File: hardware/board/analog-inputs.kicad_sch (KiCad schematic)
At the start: 17 parts, among them U5 MCP6002

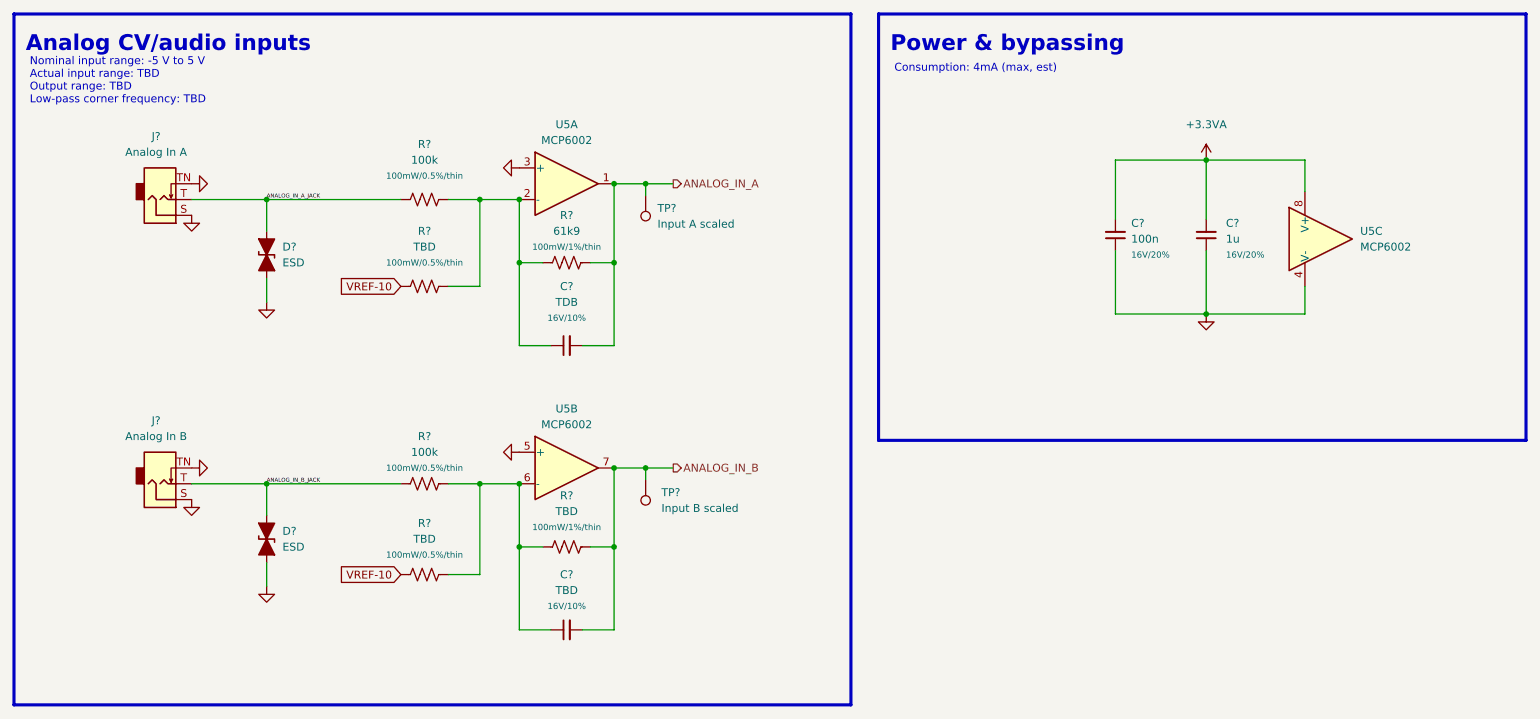
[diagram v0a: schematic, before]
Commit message: hardware: change USB connector, change flash chip, change SPI flash pin assignments, other small updates to routing
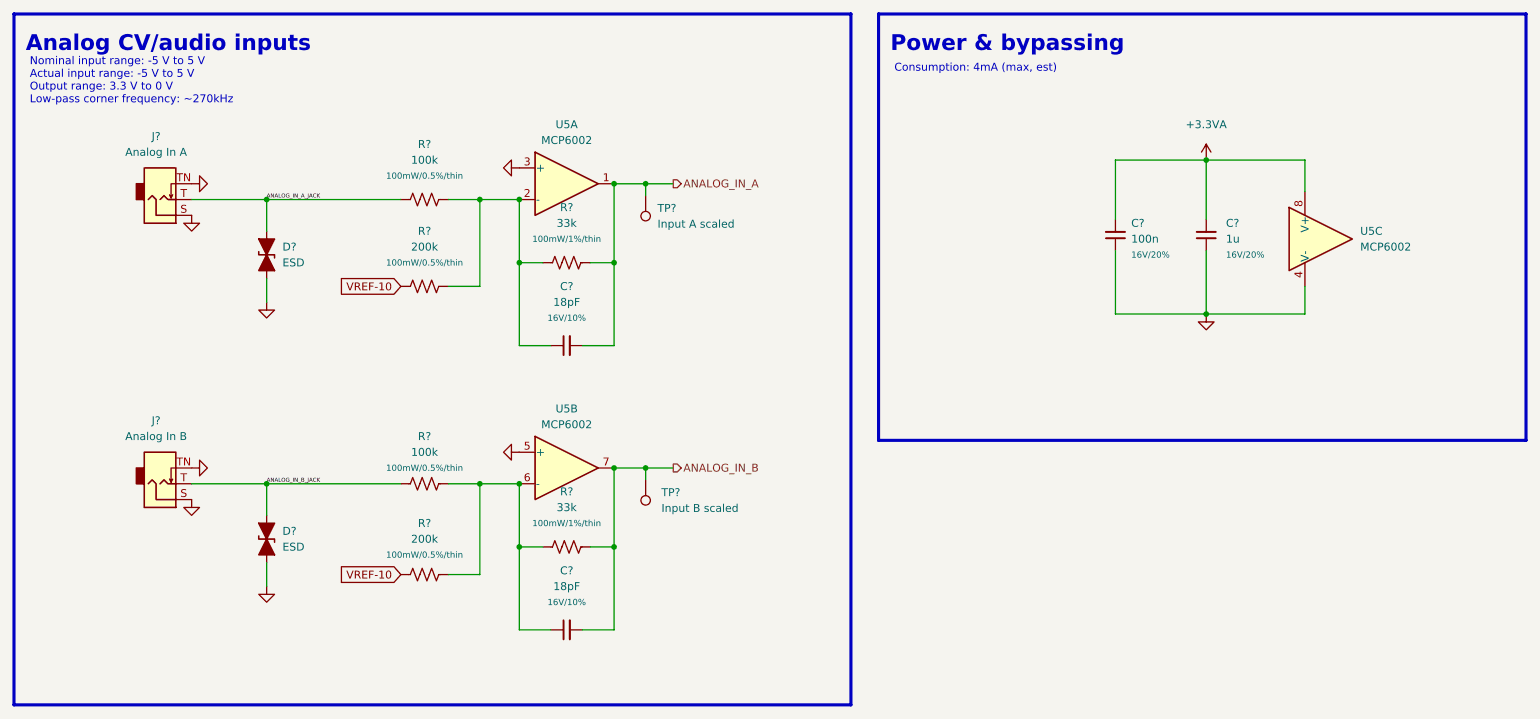
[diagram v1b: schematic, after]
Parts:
- C?: value TDB -> 18pF
- C?: value TBD -> 18pF
- R?: value TBD -> 33k
- R? (x2): value TBD -> 200k
- R?: value 61k9 -> 33k
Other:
- note added: "Nominal input range: -5 V to 5 V Actual input range: -5 V to 5 V Output range: 3.3 V to 0 V Low-pass corner frequency: ~270kHz"
- note removed: "Nominal input range: -5 V to 5 V Actual input range: TBD Output range: TBD Low-pass corner frequency: TBD"
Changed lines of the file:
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@@
     (stroke (width 0) (type default))
   )
-  (text "Nominal input range: -5 V to 5 V\nActual input range: TBD\nOutput range: TBD\nLow-pass corner frequency: TBD\n"
+  (text "Nominal input range: -5 V to 5 V\nActual input range: -5 V to 5 V\nOutput range: 3.3 V to 0 V\nLow-pass corner frequency: ~270kHz\n"
     (at 17.78 29.21 0)
     (effects (font (size 1.27 1.27)) (justify left bottom))
@@
       (effects (font (size 1.27 1.27)))
     )
-    (property "Value" "TDB" (at 104.1463 60.96 90)
+    (property "Value" "18pF" (at 104.1463 60.96 90)
       (effects (font (size 1.27 1.27)))
     )
@@
   (symbol (lib_id "Device:C_Small") (at 104.14 113.665 90) (unit 1)
     (in_bom yes) (on_board yes) (dnp no) (fields_autoplaced)
-    (property "Reference" "C?" (at 104.1463 104.775 90)
-      (effects (font (size 1.27 1.27)))
-    )
-    (property "Value" "TBD" (at 104.1463 107.315 90)
+    (property "Reference" "C?" (at 104.1463 104.14 90)
+      (effects (font (size 1.27 1.27)))
+    )
+    (property "Value" "18pF" (at 104.1463 106.68 90)
       (effects (font (size 1.27 1.27)))
     )
@@
       (effects (font (size 1.27 1.27)) hide)
     )
-    (property "Rating" "16V/10%" (at 104.1463 109.855 90)
+    (property "Rating" "16V/10%" (at 104.1463 109.22 90)
       (effects (font (size 1 1)))
     )
@@
   (symbol (lib_id "Device:R_US") (at 104.14 100.33 270) (unit 1)
     (in_bom yes) (on_board yes) (dnp no) (fields_autoplaced)
-    (property "Reference" "R?" (at 104.14 92.075 90)
-      (effects (font (size 1.27 1.27)))
-    )
-    (property "Value" "TBD" (at 104.14 94.615 90)
+    (property "Reference" "R?" (at 104.14 91.44 90)
+      (effects (font (size 1.27 1.27)))
+    )
+    (property "Value" "33k" (at 104.14 93.98 90)
       (effects (font (size 1.27 1.27)))
     )
@@
       (effects (font (size 1.27 1.27)) hide)
     )
-    (property "Rating" "100mW/1%/thin" (at 104.14 97.155 90)
+    (property "Rating" "100mW/1%/thin" (at 104.14 96.52 90)
       (effects (font (size 1 1)))
     )
@@
       (effects (font (size 1.27 1.27)))
     )
-    (property "Value" "TBD" (at 81.28 99.06 90)
+    (property "Value" "200k" (at 81.28 99.06 90)
       (effects (font (size 1.27 1.27)))
     )
@@
   (symbol (lib_id "Device:R_US") (at 104.14 54.61 270) (unit 1)
     (in_bom yes) (on_board yes) (dnp no) (fields_autoplaced)
-    (property "Reference" "R?" (at 104.14 46.99 90)
-      (effects (font (size 1.27 1.27)))
-    )
-    (property "Value" "61k9" (at 104.14 49.53 90)
+    (property "Reference" "R?" (at 104.14 45.72 90)
+      (effects (font (size 1.27 1.27)))
+    )
+    (property "Value" "33k" (at 104.14 48.26 90)
       (effects (font (size 1.27 1.27)))
     )
@@
       (effects (font (size 1.27 1.27)) hide)
     )
-    (property "Rating" "100mW/1%/thin" (at 104.14 52.07 90)
+    (property "Rating" "100mW/1%/thin" (at 104.14 50.8 90)
       (effects (font (size 1 1)))
     )
@@
       (effects (font (size 1.27 1.27)))
     )
-    (property "Value" "TBD" (at 81.28 52.07 90)
-      (effects (font (size 1.27 1.27)))
-    )
+    (property "Value" "200k" (at 81.28 52.07 90)
+      (effects (font (size 1.27 1.27)))
+    )

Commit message: hardware: rename to Goosehonk Nebula, prep v7
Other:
- title: Big Honking Button -> Goosehonk Nebula
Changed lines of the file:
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@@
   (paper "USLetter")
   (title_block
-    (title "Big Honking Button")
-    (date "2023-08-02")
-    (rev "v5")
+    (title "Goosehonk Nebula")
+    (date "2023-10-08")
+    (rev "v7")
     (company "Winterbloom")
     (comment 1 "Alethea Flowers")
     (comment 2 "CERN-OHL-P V2")
+    (comment 3 "goose.wntr.dev")
   )
   (junction (at 111.76 54.61) (diameter 0) (color 0 0 0 0)
